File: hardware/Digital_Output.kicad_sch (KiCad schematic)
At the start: 4 parts, among them U16 MCP14A0052T

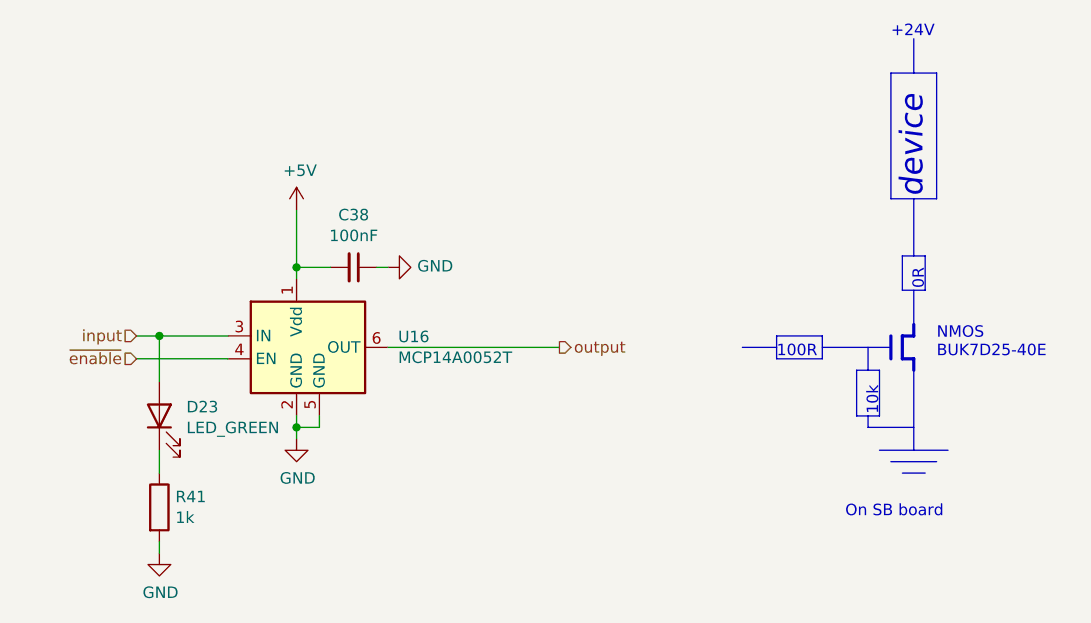
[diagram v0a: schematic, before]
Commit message: changed clock and 5v converter coils, footprints rearrange commponets to fit the need now the board connector is vertical not horizontal relative to the pcb's longest side
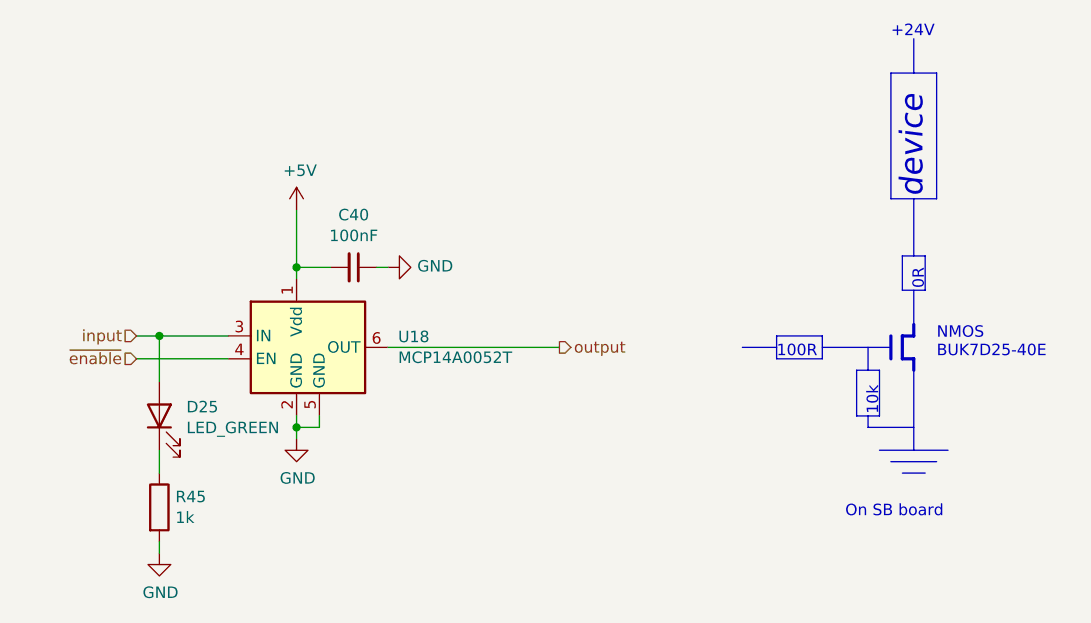
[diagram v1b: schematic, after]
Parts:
- renumbered C38 to C40, D23 to D25, R41 to R45, U16 to U18
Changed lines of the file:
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@@
   (symbol (lib_id "power:+5V") (at 121.92 97.79 0)
     (in_bom yes) (on_board yes)
-    (property "Reference" "#PWR0112" (id 0) (at 121.92 101.6 0)
+    (property "Reference" "#PWR0120" (id 0) (at 121.92 101.6 0)
       (effects (font (size 1.27 1.27)) hide)
     )
@@
   (symbol (lib_id "power:GND") (at 121.92 123.19 0)
     (in_bom yes) (on_board yes)
-    (property "Reference" "#PWR0113" (id 0) (at 121.92 129.54 0)
+    (property "Reference" "#PWR0121" (id 0) (at 121.92 129.54 0)
       (effects (font (size 1.27 1.27)) hide)
     )
@@
   (symbol (lib_id "Device:LED") (at 106.68 120.65 90)
     (in_bom yes) (on_board yes)
-    (property "Reference" "D23" (id 0) (at 109.6772 119.6594 90)
+    (property "Reference" "D25" (id 0) (at 109.6772 119.6594 90)
       (effects (font (size 1.27 1.27)) (justify right))
     )
@@
   (symbol (lib_id "Device:R") (at 106.68 130.81 0)
     (in_bom yes) (on_board yes)
-    (property "Reference" "R41" (id 0) (at 108.458 129.6416 0)
+    (property "Reference" "R45" (id 0) (at 108.458 129.6416 0)
       (effects (font (size 1.27 1.27)) (justify left))
     )
@@
   (symbol (lib_id "power:GND") (at 106.68 135.89 0)
     (in_bom yes) (on_board yes)
-    (property "Reference" "#PWR0114" (id 0) (at 106.68 142.24 0)
+    (property "Reference" "#PWR0122" (id 0) (at 106.68 142.24 0)
       (effects (font (size 1.27 1.27)) hide)
     )
@@
   (symbol (lib_id "Device:C_Small") (at 128.27 104.14 270)
     (in_bom yes) (on_board yes)
-    (property "Reference" "C38" (id 0) (at 128.27 98.3234 90))
+    (property "Reference" "C40" (id 0) (at 128.27 98.3234 90))
     (property "Value" "100nF" (id 1) (at 128.27 100.6348 90))
     (property "Footprint" "Capacitor_SMD:C_0603_1608Metric" (id 2) (at 128.27 104.14 0)
@@
   (symbol (lib_id "power:GND") (at 132.08 104.14 90)
     (in_bom yes) (on_board yes)
-    (property "Reference" "#PWR0115" (id 0) (at 138.43 104.14 0)
+    (property "Reference" "#PWR0123" (id 0) (at 138.43 104.14 0)
       (effects (font (size 1.27 1.27)) hide)
     )
@@
   (symbol (lib_id "SB-Spoko-Bezpieczniki-rescue:MCP14A0052T-MCP14A0052T") (at 121.92 113.03 0)
     (in_bom yes) (on_board yes)
-    (property "Reference" "U16" (id 0) (at 133.1976 111.8616 0)
+    (property "Reference" "U18" (id 0) (at 133.1976 111.8616 0)
       (effects (font (size 1.27 1.27)) (justify left))
     )

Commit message: minor improvements
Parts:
- renumbered C40 to C39, D25 to D24, R45 to R43, U18 to U17
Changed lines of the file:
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@@
   (symbol (lib_id "power:+5V") (at 121.92 97.79 0)
     (in_bom yes) (on_board yes)
-    (property "Reference" "#PWR0120" (id 0) (at 121.92 101.6 0)
+    (property "Reference" "#PWR0116" (id 0) (at 121.92 101.6 0)
       (effects (font (size 1.27 1.27)) hide)
     )
@@
   (symbol (lib_id "power:GND") (at 121.92 123.19 0)
     (in_bom yes) (on_board yes)
-    (property "Reference" "#PWR0121" (id 0) (at 121.92 129.54 0)
+    (property "Reference" "#PWR0117" (id 0) (at 121.92 129.54 0)
       (effects (font (size 1.27 1.27)) hide)
     )
@@
   (symbol (lib_id "Device:LED") (at 106.68 120.65 90)
     (in_bom yes) (on_board yes)
-    (property "Reference" "D25" (id 0) (at 109.6772 119.6594 90)
+    (property "Reference" "D24" (id 0) (at 109.6772 119.6594 90)
       (effects (font (size 1.27 1.27)) (justify right))
     )
@@
   (symbol (lib_id "Device:R") (at 106.68 130.81 0)
     (in_bom yes) (on_board yes)
-    (property "Reference" "R45" (id 0) (at 108.458 129.6416 0)
+    (property "Reference" "R43" (id 0) (at 108.458 129.6416 0)
       (effects (font (size 1.27 1.27)) (justify left))
     )
@@
   (symbol (lib_id "power:GND") (at 106.68 135.89 0)
     (in_bom yes) (on_board yes)
-    (property "Reference" "#PWR0122" (id 0) (at 106.68 142.24 0)
+    (property "Reference" "#PWR0118" (id 0) (at 106.68 142.24 0)
       (effects (font (size 1.27 1.27)) hide)
     )
@@
   (symbol (lib_id "Device:C_Small") (at 128.27 104.14 270)
     (in_bom yes) (on_board yes)
-    (property "Reference" "C40" (id 0) (at 128.27 98.3234 90))
+    (property "Reference" "C39" (id 0) (at 128.27 98.3234 90))
     (property "Value" "100nF" (id 1) (at 128.27 100.6348 90))
     (property "Footprint" "Capacitor_SMD:C_0603_1608Metric" (id 2) (at 128.27 104.14 0)
@@
   (symbol (lib_id "power:GND") (at 132.08 104.14 90)
     (in_bom yes) (on_board yes)
-    (property "Reference" "#PWR0123" (id 0) (at 138.43 104.14 0)
+    (property "Reference" "#PWR0119" (id 0) (at 138.43 104.14 0)
       (effects (font (size 1.27 1.27)) hide)
     )
@@
   (symbol (lib_id "SB-Spoko-Bezpieczniki-rescue:MCP14A0052T-MCP14A0052T") (at 121.92 113.03 0)
     (in_bom yes) (on_board yes)
-    (property "Reference" "U18" (id 0) (at 133.1976 111.8616 0)
+    (property "Reference" "U17" (id 0) (at 133.1976 111.8616 0)
       (effects (font (size 1.27 1.27)) (justify left))
     )

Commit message: preproduction bug fixes
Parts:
- removed C39: 100nF, Capacitor_SMD:C_0603_1608Metric, symbol Device:C_Small
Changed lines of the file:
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@@
     (pin "1")
-  )
-  (symbol (lib_id "Device:C_Small") (at 128.27 104.14 270)
-    (in_bom yes) (on_board yes)
-    (property "Reference" "C39" (id 0) (at 128.27 98.3234 90))
-    (property "Value" "100nF" (id 1) (at 128.27 100.6348 90))
-    (property "Footprint" "Capacitor_SMD:C_0603_1608Metric" (id 2) (at 128.27 104.14 0)
-      (effects (font (size 1.27 1.27)) hide)
-    )
-    (property "Datasheet" "~" (id 3) (at 128.27 104.14 0)
-      (effects (font (size 1.27 1.27)) hide)
-    )
-    (pin "1")
-    (pin "2")
   )
   (symbol (lib_id "power:GND") (at 132.08 104.14 90)
